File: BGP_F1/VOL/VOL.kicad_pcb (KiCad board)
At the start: 2 copper layers, 38 x 30 mm, 27 parts, among them P1 CONN_01X05, P2 CONN_01X05, P3 CONN_01X05, P4 CONN_01X03, P5 CONN_01X02, P6 CONN_02X02, P7 CONN_01X12, U1 MC33178, U2 MC33178

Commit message: New F0 Version
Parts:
- P1, P2, P3: footprint Connectors_Molex:Molex_MicroLatch-53253-0570_05x2.00mm_Straight -> Connectors_JST:JST_PH_B5B-PH-K_05x2.00mm_Straight
- moved P7 1.14 mm to (161.0, 78.8)
- moved P5 0.85 mm to (166.6, 93.5)
- moved P4 0.52 mm to (166.6, 99.2)
- moved P2 0.10 mm to (142.0, 103.1)
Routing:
- net /OUT: track 20.9 -> 22.7 mm
- net /PB1_1: track 22.2 -> 23.8 mm
- net /PB1_2: track 16.8 -> 18.4 mm
- net /PB2_1: track 14.7 -> 16.1 mm
- net /PB2_2: track 14.1 -> 15.4 mm
- net /PV_3: track 17.4 -> 18.6 mm
- net Earth: track 28.8 -> 29.3 mm

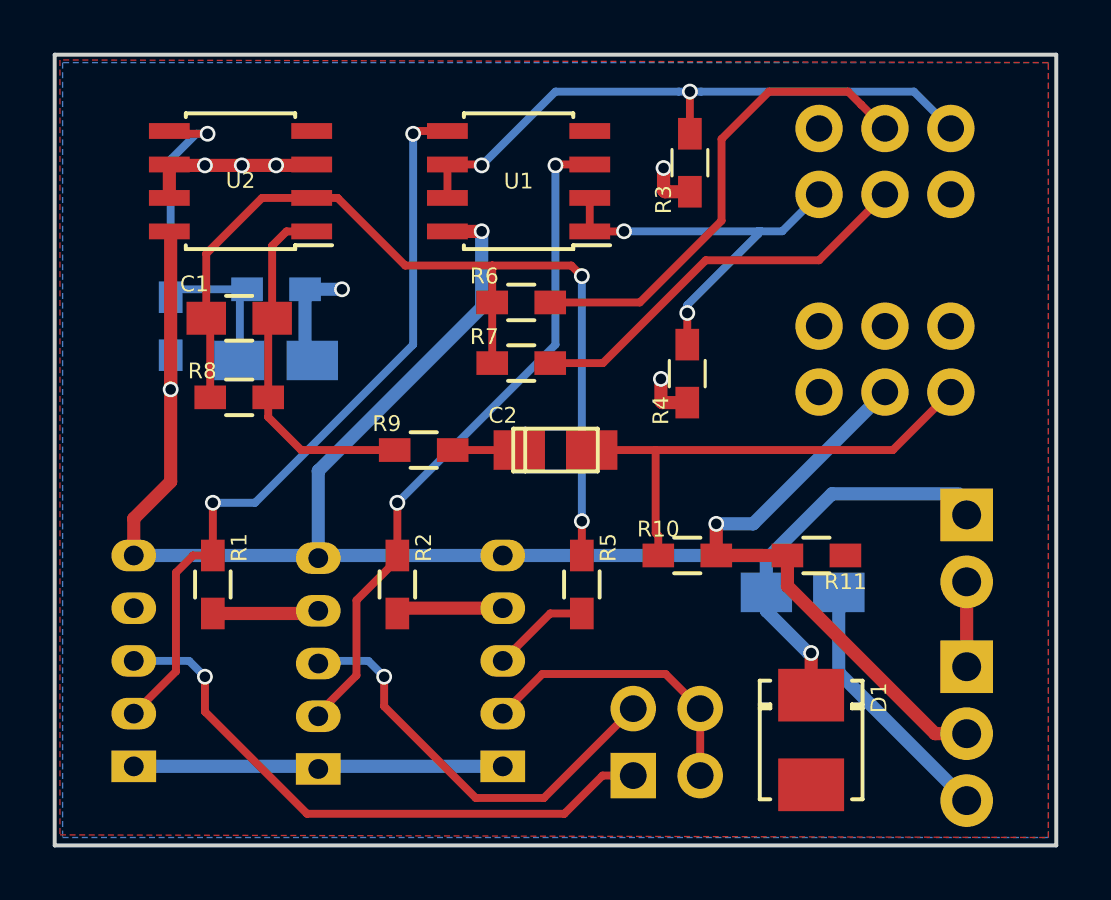
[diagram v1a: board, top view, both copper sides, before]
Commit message: F1 updates to reverse pots
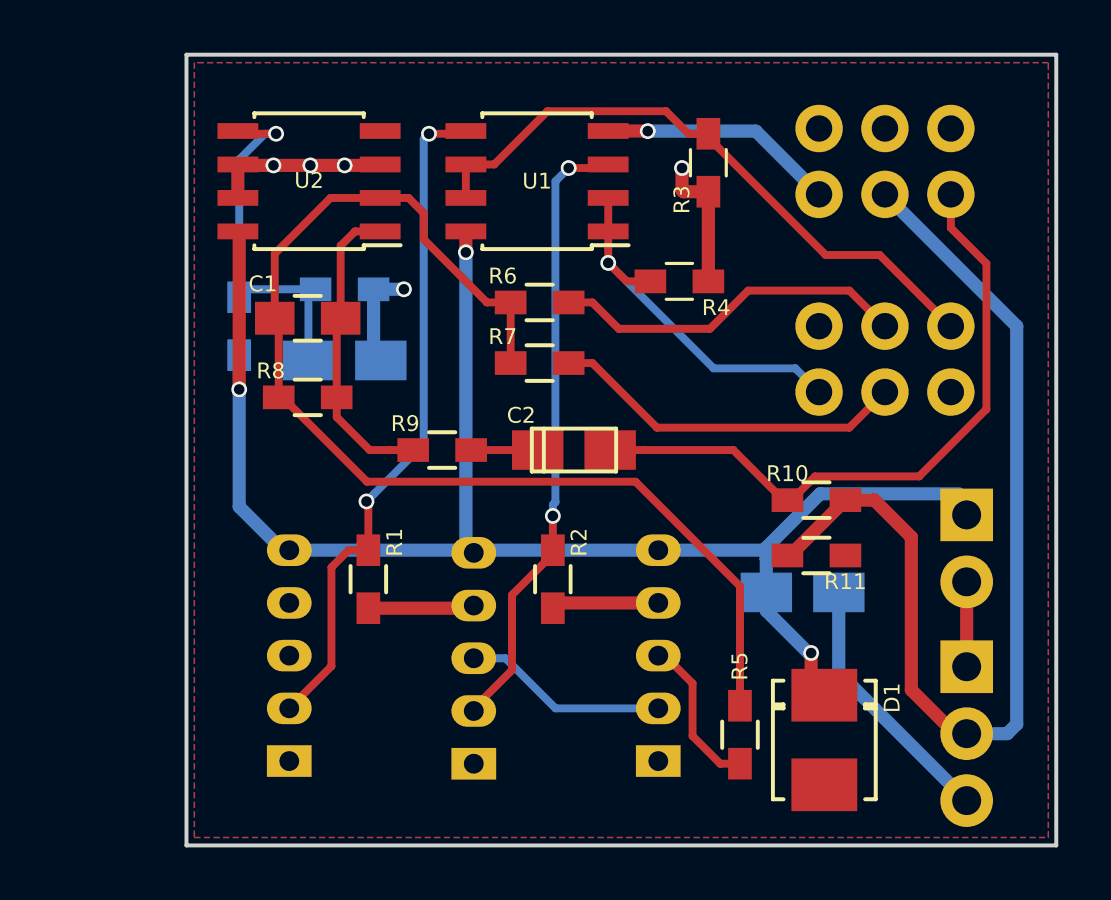
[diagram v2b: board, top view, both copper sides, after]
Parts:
- removed P6: CONN_02X02, Pin_Headers:Pin_Header_Straight_2x02
- R5, R6, R7, R8: value 4.99k -> 4.7k
- moved R5 8.28 mm to (158.0, 101.8)
- moved P1 5.90 mm to (140.9, 102.8)
- moved P3 5.90 mm to (154.9, 102.8)
- moved P2 5.90 mm to (147.9, 102.9)
- moved R1 5.90 mm to (143.9, 95.9)
- moved R2 5.90 mm to (150.9, 95.9)
- moved R10 5.33 mm to (160.9, 92.9)
- moved R4 3.51 mm to (155.7, 84.6), turned to 180 degrees
- moved C1 2.60 mm to (141.6, 86.0)
- moved C3 2.60 mm to (143.0, 87.6)
- moved R12 2.60 mm to (139.0, 86.3)
- moved R13 2.60 mm to (143.0, 84.9)
- moved R8 2.60 mm to (141.6, 89.0)
- moved U2 2.60 mm to (141.7, 80.8)
- moved R3 0.70 mm to (156.8, 80.1)
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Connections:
- P3 pad 2: /IN_HPF -> /BUF_B
- P7 pad 1: /Vref -> Net-(P7-Pad1)
- P7 pad 10: Earth -> /PB2_1
- P7 pad 11: /OUT -> /PB2_2
- P7 pad 12: /PV_3 -> /Vref
- P7 pad 2: /PB1_2 -> Net-(P7-Pad2)
- P7 pad 3: /PB1_1 -> Net-(P7-Pad3)
- P7 pad 4: /PB2_1 -> Earth
- P7 pad 5: /PB2_2 -> /OUT
- P7 pad 6: /Vref -> /PV_3
- P7 pad 7: Net-(P7-Pad7) -> /Vref
- P7 pad 8: Net-(P7-Pad8) -> /PB1_2
- P7 pad 9: Net-(P7-Pad9) -> /PB1_1
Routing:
- net /BUF_N: track 22.7 -> 0.00 mm, vias 1 -> 0
- net /OUT: track 22.7 -> 39.0 mm, vias 1 -> 0
- net /IN_HPF: track 11.4 -> 0.00 mm
- net /V+: track 69.5 -> 59.8 mm
- net Net-(C1-Pad2): track 36.3 -> 44.9 mm, vias 2 -> 0
- net /BUF_B: track 16.2 -> 7.99 mm, vias 1 -> 0
- net /PV_3: track 18.6 -> 25.2 mm
- net Earth: track 29.3 -> 23.7 mm, vias 1 -> 2
- net /PB1_2: track 18.4 -> 13.7 mm
- net /OUT_N: track 29.1 -> 25.9 mm
- net /OUT_B: track 25.8 -> 23.5 mm
- net /OUT_HPF: track 3.75 -> 5.97 mm
- net Net-(C1-Pad1): track 13.6 -> 11.7 mm
- net /PB2_2: track 15.4 -> 13.6 mm
- net /PB2_1: track 16.1 -> 14.4 mm, vias 2 -> 1
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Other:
- board size 38 x 30 mm -> 33 x 30 mm

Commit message: HPF Done
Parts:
- removed P7: CONN_01X12, LIBS:Potentiometer_Alps_RK097_Quad_Vertical_Dual_Shaft
- removed R12, R13: 100k, Resistors_SMD:R_0603_HandSoldering
- added P6: CONN_01X12, LIBS:Potentiometer_Alps_RK097_Quad_Vertical_Dual_Shaft, B.Cu at (155.5, 79.0)
- C1: footprint Capacitors_SMD:C_0805_HandSoldering -> Capacitors_SMD:C_0805; moved to B.Cu
- C3, P1, P2, P3: moved to F.Cu
- D1: footprint Diodes_SMD:DO-214BA -> Diodes_SMD:SOD-123; moved to B.Cu
- R1, R2: value 249k -> 100; footprint Resistors_SMD:R_0603_HandSoldering -> Resistors_SMD:R_0603
- R10: value 10k -> 100k; footprint Resistors_SMD:R_0603_HandSoldering -> Resistors_SMD:R_0603
- R11: value 12k -> 100k; footprint Resistors_SMD:R_0603_HandSoldering -> Resistors_SMD:R_0603
- R3, R4: value 11.1k -> 47k; footprint Resistors_SMD:R_0603_HandSoldering -> Resistors_SMD:R_0603; moved to B.Cu
- R5, R6: value 4.7k -> 47k; footprint Resistors_SMD:R_0603_HandSoldering -> Resistors_SMD:R_0603; moved to B.Cu
- R7: value 4.7k -> 100; footprint Resistors_SMD:R_0603_HandSoldering -> Resistors_SMD:R_0603
- R8: value 4.7k -> 10k; footprint Resistors_SMD:R_0603_HandSoldering -> Resistors_SMD:R_0603
- R9: value 100 -> 12k; footprint Resistors_SMD:R_0603_HandSoldering -> Resistors_SMD:R_0603
- U2: moved to B.Cu
- moved R11 25.3 mm to (142.7, 77.4)
- moved R8 24.7 mm to (164.9, 80.8), turned to 0 degrees
- moved R9 23.5 mm to (167.9, 80.8), turned to 0 degrees
- moved R10 20.8 mm to (147.0, 77.4), turned to 180 degrees
- moved C2 19.7 mm to (166.5, 78.0), turned to 0 degrees
- moved R3 18.2 mm to (139.7, 86.3), turned to 180 degrees
- moved R5 17.3 mm to (150.4, 86.3), turned to 0 degrees
- moved P3 16.0 mm to (139.7, 97.8)
- moved R4 10.8 mm to (145.0, 86.3), turned to 0 degrees
- moved R7 10.3 mm to (150.9, 77.4), turned to 180 degrees
- moved R1 9.66 mm to (145.0, 86.3), turned to 180 degrees
- moved R2 9.61 mm to (150.4, 86.3), turned to 180 degrees
- moved D1 7.92 mm to (155.8, 96.2)
- moved C1 7.80 mm to (147.5, 80.9), turned to 90 degrees
- moved C3 6.69 mm to (140.5, 81.4), turned to 90 degrees
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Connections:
- P3 pad 2: /BUF_B -> /BUF_N
- R1 pad 1: /OUT_N -> Net-(R1-Pad1)
- R1 pad 2: /Vref -> /OUT_N
- R10 pad 1: /PV_3 -> /V+
- R10 pad 2: /OUT -> Net-(C3-Pad1)
- R11 pad 1: /OUT -> Net-(C3-Pad1)
- R2 pad 1: /OUT_B -> Net-(R2-Pad1)
- R2 pad 2: /Vref -> /OUT_B
- R3 pad 1: /Vref -> Net-(C1-Pad2)
- R3 pad 2: /PB1_1 -> /OUT_HPF
- R4 pad 1: /Vref -> Net-(C1-Pad2)
- R4 pad 2: /PB2_1 -> /PB1_2
- R5 pad 2: /OUT_HPF -> /PB2_2
- R6 pad 1: Net-(C1-Pad2) -> Net-(C1-Pad1)
- R6 pad 2: /PB1_2 -> Net-(C1-Pad2)
- R7 pad 1: Net-(C1-Pad2) -> Net-(C2-Pad1)
- R7 pad 2: /PB2_2 -> Net-(C1-Pad1)
- R8 pad 1: Net-(C1-Pad1) -> /PV_3
- R8 pad 2: Net-(C1-Pad2) -> /OUT
- R9 pad 1: Net-(C2-Pad1) -> /OUT
- R9 pad 2: Net-(C1-Pad1) -> Earth
- U1 pad 1: /PB2_1 -> /PB1_1
- U1 pad 2: /PB2_1 -> /PB1_1
- U1 pad 3: /OUT_B -> Net-(R1-Pad1)
- U1 pad 5: /OUT_N -> Net-(R2-Pad1)
- U1 pad 6: /PB1_1 -> /PB2_1
- U1 pad 7: /PB1_1 -> /PB2_1
- U2 pad 1: Net-(C1-Pad1) -> /Vref
- U2 pad 2: Net-(C1-Pad2) -> /Vref
- U2 pad 3: /Vref -> Net-(C3-Pad1)
- U2 pad 5: Net-(C3-Pad1) -> /Vref
- U2 pad 6: /Vref -> Net-(C1-Pad2)
- U2 pad 7: /Vref -> Net-(C1-Pad1)
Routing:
- net Net-(C1-Pad2): track 44.9 -> 22.7 mm
- net /Vref: track 20.1 -> 0.00 mm, vias 4 -> 0
- net /PV_3: track 25.2 -> 7.28 mm
- net /OUT_N: track 25.9 -> 11.0 mm, vias 2 -> 1
- net Net-(C2-Pad1): track 2.53 -> 17.3 mm
- net /OUT_B: track 23.5 -> 11.0 mm, vias 2 -> 1
- net /OUT: track 39.0 -> 27.9 mm
- net Earth: track 23.7 -> 32.4 mm, vias 2 -> 1
- net /BUF_B: track 7.99 -> 0.00 mm
- net /BUF_N: track 0.00 -> 6.33 mm
- net Net-(R1-Pad1): track 0.00 -> 5.60 mm
- net /V+: track 59.8 -> 55.1 mm, vias 3 -> 2
- net Net-(R2-Pad1): track 0.00 -> 3.97 mm
- net /PB2_2: track 13.6 -> 10.1 mm, vias 0 -> 1
- net /PB2_1: track 14.4 -> 11.0 mm, vias 1 -> 0
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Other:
- board size 33 x 30 mm -> 33 x 25 mm
